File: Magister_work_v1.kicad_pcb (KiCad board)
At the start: 2 copper layers, 17 parts, among them J1 Conn_01x04_Pin, J2 Conn_01x03_Pin, J3 Conn_01x03_Pin, J4 Conn_01x03_Pin, J5 Conn_01x03_Pin, J6 Conn_01x04_Pin, U1 LM66100DCK, U2 XC6206P332MR

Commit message: feat: firs complete version schemattic
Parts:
- added C10: 10u, Capacitor_SMD:C_0805_2012Metric, F.Cu at (218.2, 74.2)
- added C11: 1u, Capacitor_SMD:C_0805_2012Metric, F.Cu at (218.2, 77.2)
- added C12: 15p, Capacitor_SMD:C_0805_2012Metric_Pad1.18x1.45mm_HandSolder, F.Cu at (212.0, 85.7)
- added C13: 15p, Capacitor_SMD:C_0805_2012Metric_Pad1.18x1.45mm_HandSolder, F.Cu at (212.0, 88.7)
- added C14: 10u, Capacitor_SMD:C_0805_2012Metric_Pad1.18x1.45mm_HandSolder, F.Cu at (212.0, 91.7)
- added C15: 1u, Capacitor_SMD:C_0805_2012Metric_Pad1.18x1.45mm_HandSolder, F.Cu at (212.0, 94.7)
- added C16: 1u, Capacitor_SMD:C_0805_2012Metric_Pad1.18x1.45mm_HandSolder, F.Cu at (212.0, 97.7)
- added C17: 1u, Capacitor_SMD:C_0805_2012Metric_Pad1.18x1.45mm_HandSolder, F.Cu at (212.0, 100.7)
- added C18: 0.1u, Capacitor_SMD:C_0805_2012Metric_Pad1.18x1.45mm_HandSolder, F.Cu at (212.0, 103.7)
- added C19: 2.2u, Capacitor_SMD:C_0805_2012Metric_Pad1.18x1.45mm_HandSolder, F.Cu at (212.0, 106.7)
- added C20: 0.1u, Capacitor_SMD:C_0805_2012Metric_Pad1.18x1.45mm_HandSolder, F.Cu at (174.4, 55.0)
- added C21: 0.1u, Capacitor_SMD:C_0805_2012Metric_Pad1.18x1.45mm_HandSolder, F.Cu at (174.4, 58.0)
- added C22: 22n, Capacitor_SMD:C_0805_2012Metric_Pad1.18x1.45mm_HandSolder, F.Cu at (174.4, 61.0)
- added C23: 0.1u, Capacitor_SMD:C_0805_2012Metric_Pad1.18x1.45mm_HandSolder, F.Cu at (174.4, 64.0)
- added C24: 0.1u, Capacitor_SMD:C_0805_2012Metric_Pad1.18x1.45mm_HandSolder, F.Cu at (174.4, 67.0)
- added C25: 0.1u, Capacitor_SMD:C_0805_2012Metric_Pad1.18x1.45mm_HandSolder, F.Cu at (174.4, 70.1)
- added C26: 0.1u, Capacitor_SMD:C_0805_2012Metric_Pad1.18x1.45mm_HandSolder, F.Cu at (174.4, 73.1)
- added C27: 0.1u, Capacitor_SMD:C_0805_2012Metric_Pad1.18x1.45mm_HandSolder, F.Cu at (174.4, 76.1)
- added C28: 0.1u, Capacitor_SMD:C_0805_2012Metric_Pad1.18x1.45mm_HandSolder, F.Cu at (174.4, 79.1)
- added C29: 0.1u, Capacitor_SMD:C_0805_2012Metric_Pad1.18x1.45mm_HandSolder, F.Cu at (222.9, 74.0)
- added C30: 0.1u, Capacitor_SMD:C_0805_2012Metric_Pad1.18x1.45mm_HandSolder, F.Cu at (222.9, 77.0)
- added C7: 10u, Capacitor_SMD:C_0805_2012Metric, F.Cu at (218.2, 65.2)
- added C8: 1u, Capacitor_SMD:C_0805_2012Metric, F.Cu at (218.2, 68.2)
- added C9: 10u, Capacitor_SMD:C_0805_2012Metric, F.Cu at (218.2, 71.2)
- added D2: SMBJ5.0CA, Diode_SMD:D_SMB_Handsoldering, F.Cu at (195.4, 80.8)
- added D3: SMBJ5.0CA, Diode_SMD:D_SMB_Handsoldering, F.Cu at (195.4, 86.3)
- added D4: BAT54C, Package_TO_SOT_SMD:SOT-23_Handsoldering, F.Cu at (212.8, 56.0)
- added DA1: K7803-500R3, Package_SIP:SIP3_11.6x8.5mm, F.Cu at (220.1, 60.8)
- added DD2: MPU-6050, Sensor_Motion:InvenSense_QFN-24_4x4mm_P0.5mm, F.Cu at (166.8, 94.0)
- added DD3: BMP280, Package_LGA:Bosch_LGA-8_2x2.5mm_P0.65mm_ClockwisePinNumbering, F.Cu at (202.9, 86.4)
- added J10: Conn_01x02_Pin, Connector_Hirose:Hirose_DF13-02P-1.25DSA_1x02_P1.25mm_Vertical, F.Cu at (227.7, 66.9)
- added J6: Conn_01x04_Pin, Connector_PinSocket_2.54mm:PinSocket_1x04_P2.54mm_Vertical, F.Cu at (216.7, 86.4)
- added J7: Conn_01x04_Pin, Connector_PinHeader_2.54mm:PinHeader_1x04_P2.54mm_Horizontal, F.Cu at (179.1, 74.8)
- added J8: Conn_01x06_Pin, Connector_Hirose:Hirose_DF13-06P-1.25DSA_1x06_P1.25mm_Vertical, F.Cu at (192.6, 75.8)
- added J9: Conn_01x02_Pin, Connector_Hirose:Hirose_DF13-02P-1.25DSA_1x02_P1.25mm_Vertical, F.Cu at (203.8, 75.8)
- added R1: 10k, Resistor_SMD:R_0805_2012Metric_Pad1.20x1.40mm_HandSolder, F.Cu at (221.3, 85.6)
- added R10: 1k, Resistor_SMD:R_0805_2012Metric_Pad1.20x1.40mm_HandSolder, F.Cu at (222.8, 68.1)
- added R11: 10k, Resistor_SMD:R_0805_2012Metric_Pad1.20x1.40mm_HandSolder, F.Cu at (222.8, 71.0)
- added R2: 10k, Resistor_SMD:R_0805_2012Metric_Pad1.20x1.40mm_HandSolder, F.Cu at (221.3, 88.6)
- added R3: 10k, Resistor_SMD:R_0805_2012Metric_Pad1.20x1.40mm_HandSolder, F.Cu at (221.3, 91.5)
- added R4: 3.3k, Resistor_SMD:R_0805_2012Metric_Pad1.20x1.40mm_HandSolder, F.Cu at (198.7, 55.0)
- added R5: 3.3k, Resistor_SMD:R_0805_2012Metric_Pad1.20x1.40mm_HandSolder, F.Cu at (198.7, 57.9)
- added R6: 3.3k, Resistor_SMD:R_0805_2012Metric_Pad1.20x1.40mm_HandSolder, F.Cu at (198.7, 60.9)
- added R7: 3.3k, Resistor_SMD:R_0805_2012Metric_Pad1.20x1.40mm_HandSolder, F.Cu at (198.7, 63.8)
- added R8: 3.3k, Resistor_SMD:R_0805_2012Metric_Pad1.20x1.40mm_HandSolder, F.Cu at (198.7, 66.8)
- added R9: 3k, Resistor_SMD:R_0805_2012Metric_Pad1.20x1.40mm_HandSolder, F.Cu at (222.8, 65.1)
- added U3: Ai-Thinker-Ra-01, RF_Module:Ai-Thinker-Ra-01-LoRa, F.Cu at (186.6, 63.0)
- added U4: MCP6001-OT, Package_TO_SOT_SMD:SOT-23-5, F.Cu at (239.9, 64.0)
- added VD1: GSOT03C-E3-08, Package_TO_SOT_SMD:SOT-23_Handsoldering, F.Cu at (204.3, 56.0)
- added VD2: GSOT03C-E3-08, Package_TO_SOT_SMD:SOT-23_Handsoldering, F.Cu at (204.3, 60.8)
- added VD3: GSOT03C-E3-08, Package_TO_SOT_SMD:SOT-23_Handsoldering, F.Cu at (204.3, 65.5)
- added VD4: GSOT03C-E3-08, Package_TO_SOT_SMD:SOT-23_Handsoldering, F.Cu at (212.8, 60.8)
- added VD5: GSOT03C-E3-08, Package_TO_SOT_SMD:SOT-23_Handsoldering, F.Cu at (212.8, 65.5)
- added VD6: GSOT03C-E3-08, Package_TO_SOT_SMD:SOT-23_Handsoldering, F.Cu at (212.8, 70.3)
- added VD7: GSOT03C-E3-08, Package_TO_SOT_SMD:SOT-23_Handsoldering, F.Cu at (212.8, 75.1)
- added VD8: GSOT03C-E3-08, Package_TO_SOT_SMD:SOT-23_Handsoldering, F.Cu at (212.8, 79.9)
- added Y1: X322525MQB4SI, Oscillator:Oscillator_SMD_Abracon_ASE-4Pin_3.2x2.5mm, F.Cu at (217.0, 98.6)
- C1: footprint Capacitor_SMD:C_0805_2012Metric -> Capacitor_SMD:C_0805_2012Metric_Pad1.18x1.45mm_HandSolder
- D1: footprint Diode_SMD:D_SMB -> Diode_SMD:D_SMB_Handsoldering
- F1: footprint Fuse:Fuse_1812_4532Metric -> Fuse:Fuse_1812_4532Metric_Pad1.30x3.40mm_HandSolder
- moved U1 103.5 mm to (145.8, 73.7)
- moved DD1 44.7 mm to (222.0, 125.5)
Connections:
- DD1 pad 1: unconnected-(DD1-VBAT-Pad1) -> +3V3D
- DD1 pad 12: unconnected-(DD1-VSSA-Pad12) -> GND
- DD1 pad 13: unconnected-(DD1-VREF+-Pad13) -> +3V3A
- DD1 pad 18: unconnected-(DD1-VSS-Pad18) -> GND
- DD1 pad 19: unconnected-(DD1-VDD-Pad19) -> +3V3D
- DD1 pad 28: unconnected-(DD1-PB2-Pad28) -> Net-(DD1-PB2)
- DD1 pad 30: unconnected-(DD1-VCAP1-Pad30) -> Net-(DD1-VCAP1)
- DD1 pad 31: unconnected-(DD1-VSS-Pad31) -> GND
- DD1 pad 32: unconnected-(DD1-VDD-Pad32) -> +3V3D
- DD1 pad 46: unconnected-(DD1-PA13-Pad46) -> Net-(DD1-PA13)
- DD1 pad 47: unconnected-(DD1-VSS-Pad47) -> GND
- DD1 pad 48: unconnected-(DD1-VDD-Pad48) -> +3V3D
- DD1 pad 49: unconnected-(DD1-PA14-Pad49) -> Net-(DD1-PA14)
- DD1 pad 5: unconnected-(DD1-PH0-Pad5) -> Net-(DD1-PH0)
- DD1 pad 6: unconnected-(DD1-PH1-Pad6) -> Net-(DD1-PH1)
- DD1 pad 60: unconnected-(DD1-BOOT0-Pad60) -> Net-(DD1-BOOT0)
- DD1 pad 63: unconnected-(DD1-VSS-Pad63) -> GND
- DD1 pad 64: unconnected-(DD1-VDD-Pad64) -> +3V3D
- DD1 pad 7: unconnected-(DD1-NRST-Pad7) -> Net-(DD1-NRST)

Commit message: feat: added all connection for MCU
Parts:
- removed the J6 at (199.7, 117.9)
- added D5: BAT54C, Package_TO_SOT_SMD:SOT-23_Handsoldering, F.Cu at (236.7, 111.0)
- added VD9: GSOT03C-E3-08, Package_TO_SOT_SMD:SOT-23_Handsoldering, F.Cu at (236.7, 115.8)
- U4: footprint Package_TO_SOT_SMD:SOT-23-5 -> Package_TO_SOT_SMD:SOT-23-5_HandSoldering
- moved J1 58.4 mm to (253.5, 120.9)
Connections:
- DD1 pad 14: unconnected-(DD1-PA0-Pad14) -> PWM1
- DD1 pad 15: unconnected-(DD1-PA1-Pad15) -> PWM2
- DD1 pad 16: unconnected-(DD1-PA2-Pad16) -> PWM3
- DD1 pad 17: unconnected-(DD1-PA3-Pad17) -> PWM4
- DD1 pad 21: unconnected-(DD1-PA5-Pad21) -> SCK_BMP280
- DD1 pad 22: unconnected-(DD1-PA6-Pad22) -> SDO_BMP280
- DD1 pad 23: unconnected-(DD1-PA7-Pad23) -> SDI_BMP280
- DD1 pad 24: unconnected-(DD1-PC4-Pad24) -> CSB_BMP280
- DD1 pad 26: unconnected-(DD1-PB0-Pad26) -> BAT_CTRL
- DD1 pad 29: unconnected-(DD1-PB10-Pad29) -> BN_880_SCL
- DD1 pad 33: unconnected-(DD1-PB12-Pad33) -> Reset_LoRa
- DD1 pad 34: unconnected-(DD1-PB13-Pad34) -> SCK_LoRa
- DD1 pad 35: unconnected-(DD1-PB14-Pad35) -> MISO_LoRa
- DD1 pad 36: unconnected-(DD1-PB15-Pad36) -> MOSI_LoRa
- DD1 pad 37: unconnected-(DD1-PC6-Pad37) -> SS_LoRa
- DD1 pad 38: unconnected-(DD1-PC7-Pad38) -> DIO0_LoRa
- DD1 pad 39: unconnected-(DD1-PC8-Pad39) -> DIO1_LoRa
- DD1 pad 40: unconnected-(DD1-PC9-Pad40) -> DIO2_LoRa
- DD1 pad 42: unconnected-(DD1-PA9-Pad42) -> BN_880_RX
- DD1 pad 43: unconnected-(DD1-PA10-Pad43) -> BN_880_TX
- DD1 pad 44: unconnected-(DD1-PA11-Pad44) -> TX_debug
- DD1 pad 45: unconnected-(DD1-PA12-Pad45) -> RX_debug
- DD1 pad 52: unconnected-(DD1-PC11-Pad52) -> HC_trigger
- DD1 pad 53: unconnected-(DD1-PC12-Pad53) -> HC_echo
- DD1 pad 55: unconnected-(DD1-PB3-Pad55) -> BN_880_SDA
- DD1 pad 57: unconnected-(DD1-PB5-Pad57) -> INT_MPU6050
- DD1 pad 58: unconnected-(DD1-PB6-Pad58) -> SCL_MPU6050
- DD1 pad 59: unconnected-(DD1-PB7-Pad59) -> SDA_MPU6050
- J1 pad 1: +5V -> Net-(J1-Pin_1)
- J1 pad 3: unconnected-(J1-Pin_3-Pad3) -> TX_debug
- J1 pad 4: unconnected-(J1-Pin_4-Pad4) -> RX_debug
- U3 pad 4: SS_LoRa -> Reset_LoRa
- U3 pad 5: MOSI_LoRa -> DIO0_LoRa
- U3 pad 6: MISO_LoRa -> DIO1_LoRa
- U3 pad 7: SCK_LoRa -> DIO2_LoRa

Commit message: feat: complete schematic, and start PCB
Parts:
- removed C26: 0.1u, Capacitor_SMD:C_0805_2012Metric_Pad1.18x1.45mm_HandSolder
- removed D1, D2, D3: SMBJ5.0CA, Diode_SMD:D_SMB_Handsoldering
- added C31: 0.1u, Capacitor_SMD:C_0805_2012Metric_Pad1.18x1.45mm_HandSolder, F.Cu at (153.9, 115.2)
- added C32: 0.1u, Capacitor_SMD:C_0805_2012Metric_Pad1.18x1.45mm_HandSolder, F.Cu at (153.9, 118.2)
- added D6: SMBJ5.0CA, Diode_SMD:D_SMB_Handsoldering, F.Cu at (94.0, 33.5)
- added D7: SMBJ5.0CA, Diode_SMD:D_SMB_Handsoldering, F.Cu at (46.5, 118.0)
- added D8: SMBJ5.0CA, Diode_SMD:D_SMB_Handsoldering, F.Cu at (39.0, 101.0)
- added D9: BAT54C, Package_TO_SOT_SMD:SOT-23_Handsoldering, F.Cu at (155.7, 105.5)
- added L1: BLM21PG121SN1D, Inductor_SMD:L_0805_2012Metric_Pad1.05x1.20mm_HandSolder, F.Cu at (160.8, 112.3)
- added L2: BLM21PG121SN1D, Inductor_SMD:L_0805_2012Metric_Pad1.05x1.20mm_HandSolder, F.Cu at (153.9, 112.3)
- C10, C11, C2, C3, C4, C5, C6, C7, C8, C9: footprint Capacitor_SMD:C_0805_2012Metric -> Capacitor_SMD:C_0805_2012Metric_Pad1.18x1.45mm_HandSolder
- C16, C17: value 1u -> 0.1u
- U2: footprint Package_TO_SOT_SMD:SOT-23-3 -> Package_TO_SOT_SMD:SOT-23_Handsoldering
- moved J1 224.5 mm to (32.0, 84.3), turned to 180 degrees
- moved U2 211.4 mm to (41.0, 31.5)
- moved J10 195.7 mm to (32.0, 69.5), turned to 90 degrees
- moved U4 194.7 mm to (45.1, 65.5), turned to 180 degrees
- moved C6 180.8 mm to (34.0, 32.0), turned to 90 degrees
- moved J9 172.6 mm to (32.0, 91.8), turned to 90 degrees
- moved DA1 170.4 mm to (52.2, 31.5), turned to -90 degrees
- moved C5 168.3 mm to (46.5, 32.0), turned to -90 degrees
- moved J8 163.1 mm to (32.0, 104.1), turned to 90 degrees
- moved DD1 159.6 mm to (67.0, 87.5)
- moved C7 158.0 mm to (63.5, 33.5), turned to 90 degrees
- moved DD3 157.1 mm to (50.0, 50.2)
- moved C8 155.2 mm to (67.0, 33.5), turned to 90 degrees
- moved F1 150.0 mm to (100.5, 30.5)
- moved J7 146.0 mm to (40.0, 119.1), turned to 180 degrees
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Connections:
- C1 pad 1: Net-(D1-A2) -> Net-(D6-A2)
- C17 pad 1: +3V3D -> +3V3_MCU
- C2 pad 1: Net-(D1-A2) -> Net-(D6-A2)
- C3 pad 1: Net-(D1-A2) -> Net-(D6-A2)
- DD1 pad 1: +3V3D -> +3V3_MCU
- DD1 pad 19: +3V3D -> +3V3_MCU
- DD1 pad 32: +3V3D -> +3V3_MCU
- DD1 pad 48: +3V3D -> +3V3_MCU
- DD1 pad 64: +3V3D -> +3V3_MCU
- F1 pad 1: (no net) -> +5V_1
- F1 pad 2: (no net) -> Net-(D6-A2)
- J6 pad 1: +3V3D -> Net-(J6-Pin_1)
- J6 pad 2: GND -> Net-(DD1-PA13)
- J6 pad 3: Net-(DD1-PA13) -> Net-(DD1-PA14)
- J6 pad 4: Net-(DD1-PA14) -> GND
- U1 pad 1: Net-(D1-A2) -> Net-(D6-A2)
- U3 pad 3: +3V3D -> Net-(U3-VDD)
- VD9 pad 1: TX_debug -> RX_debug
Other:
- board outline added: 100 x 100 mm

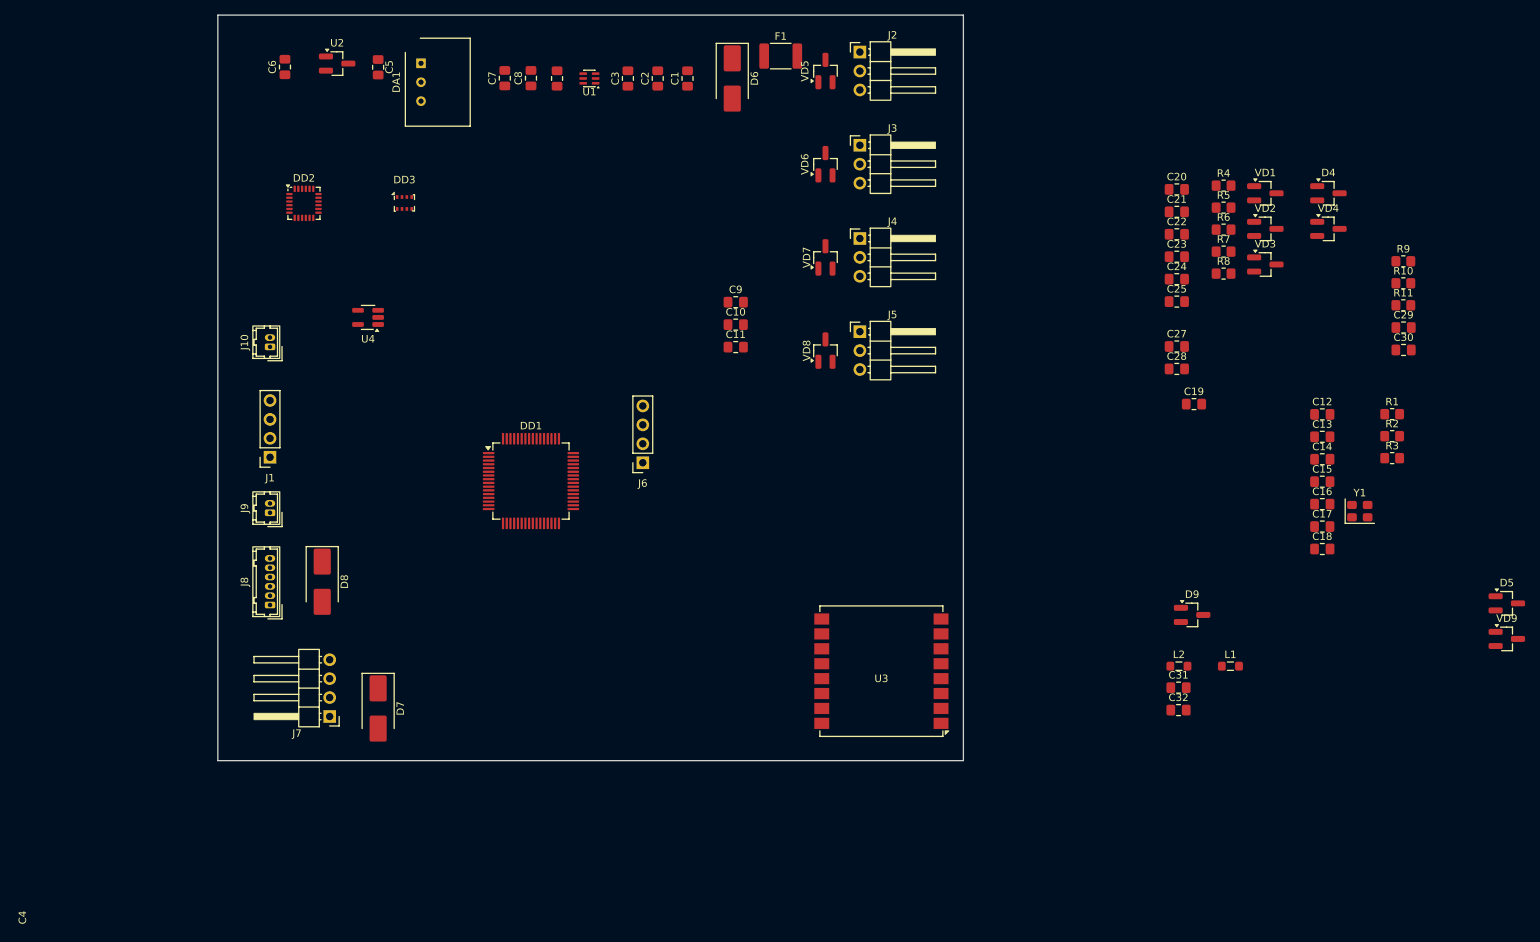
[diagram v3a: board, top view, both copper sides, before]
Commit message: feat: first version pf PCB without data and power line
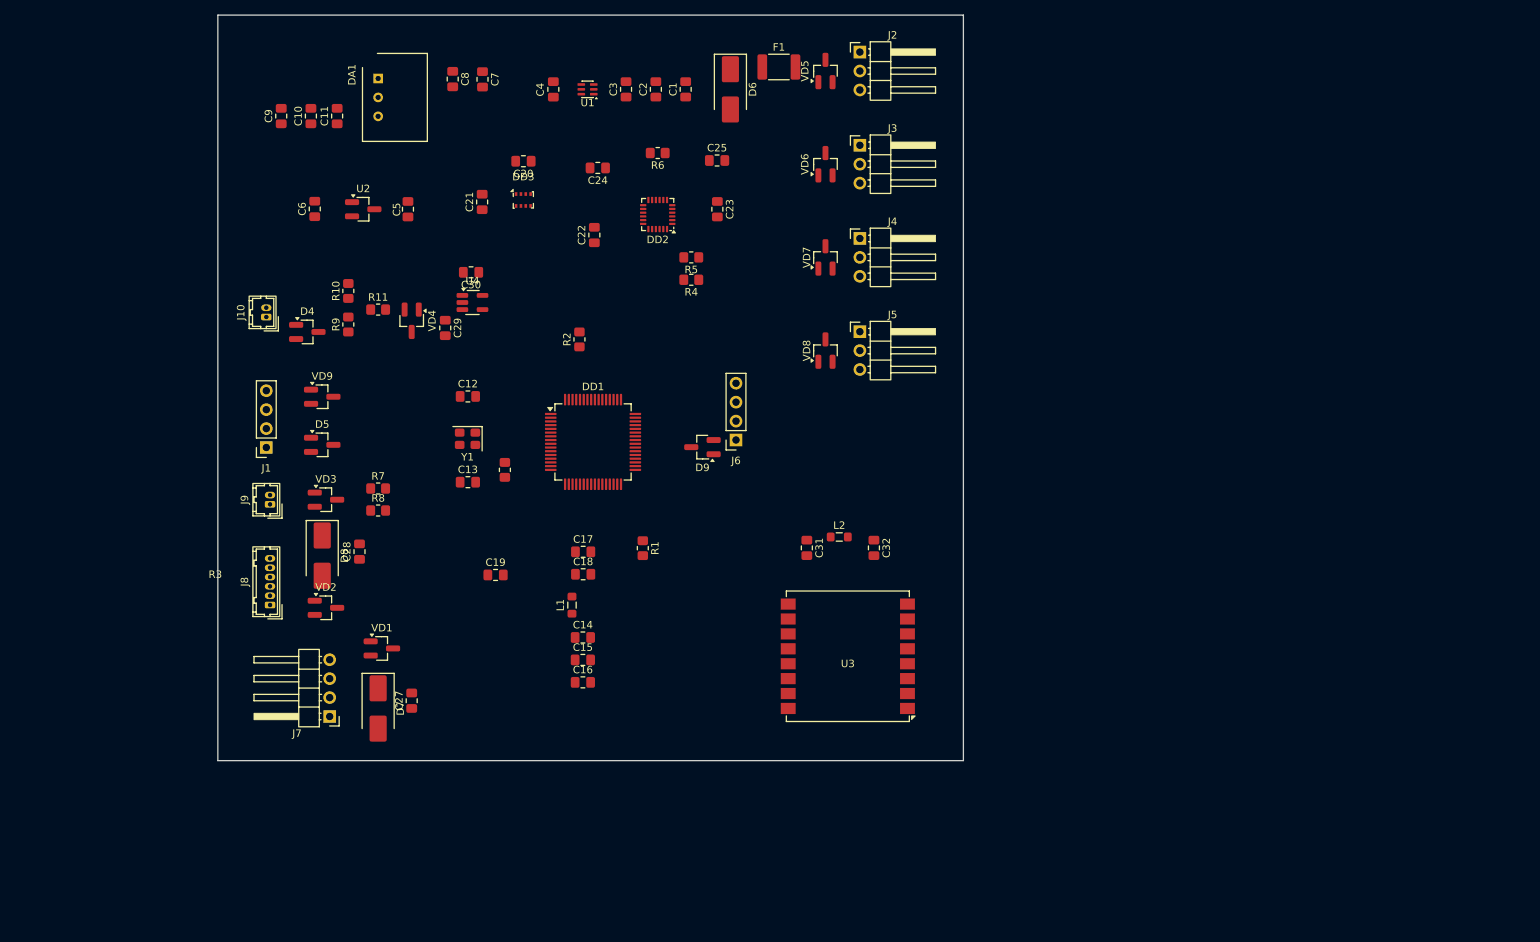
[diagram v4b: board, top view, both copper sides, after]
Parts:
- moved VD9 162.2 mm to (39.0, 76.2)
- moved D5 160.3 mm to (39.0, 82.6)
- moved R9 141.8 mm to (42.5, 66.5), turned to 90 degrees
- moved R10 141.5 mm to (42.5, 62.0), turned to 90 degrees
- moved D4 138.2 mm to (37.0, 67.5)
- moved R11 137.5 mm to (46.5, 64.5)
- moved VD2 135.9 mm to (39.5, 104.5)
- moved VD1 133.3 mm to (47.0, 110.0)
- moved VD3 129.9 mm to (39.5, 90.0)
- moved C29 128.5 mm to (55.5, 67.0), turned to -90 degrees
- moved C30 125.5 mm to (59.0, 59.5), turned to 180 degrees
- moved VD4 123.6 mm to (51.0, 66.0), turned to -90 degrees
- moved Y1 120.1 mm to (58.5, 81.8), turned to 180 degrees
- moved R3 119.0 mm to (63.5, 86.0), turned to 90 degrees
- moved R7 117.8 mm to (46.5, 88.5)
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
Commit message: feat: start PCB trace
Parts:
- moved L2 16.6 mm to (119.5, 107.3), turned to -90 degrees
- moved C32 16.3 mm to (118.0, 112.0), turned to 180 degrees
- moved C31 15.5 mm to (118.0, 103.0), turned to 180 degrees
- moved D9 13.7 mm to (103.5, 85.5), turned to 0 degrees
- moved C18 13.2 mm to (65.5, 90.0), turned to 90 degrees
- moved C6 13.0 mm to (51.0, 50.1), turned to -90 degrees
- moved R3 8.66 mm to (65.5, 94.4)
- moved C5 8.56 mm to (42.0, 50.0), turned to -90 degrees
- moved L1 6.77 mm to (78.5, 101.0), turned to 0 degrees
- moved DD1 6.72 mm to (82.0, 83.0)
- moved C14 5.43 mm to (78.5, 105.5)
- moved VD5 5.02 mm to (107.0, 37.5), turned to -90 degrees
- moved C15 4.92 mm to (78.5, 109.5)
- moved C16 4.92 mm to (78.5, 112.5)
- moved J6 4.72 mm to (98.5, 84.5)
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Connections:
- net Net-(D6-A2) renamed +5V_2
- R10 pad 1: Net-(VD4-K1) -> Net-(R10-Pad1)
- R11 pad 1: Net-(VD4-K1) -> Net-(R10-Pad1)
- R9 pad 2: Net-(VD4-K1) -> Net-(R10-Pad1)
- VD4 pad 1: Net-(VD4-K1) -> Net-(U4-+)
- VD4 pad 2: Net-(VD4-K1) -> Net-(U4-+)
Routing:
- net +5V: track 0.00 -> 65.2 mm
- net +5V_1: track 0.00 -> 56.9 mm
- net GND: track 0.00 -> 47.1 mm
- net +5V_2: track 0.00 -> 28.1 mm
- net +3V3D: track 0.00 -> 16.8 mm
- net Net-(U4-+): track 0.00 -> 14.6 mm
- net BAT_CTRL: track 0.00 -> 12.8 mm
- net Net-(U3-VDD): track 0.00 -> 11.7 mm
- net Net-(J1-Pin_1): track 0.00 -> 8.14 mm
- net BN_880_TX: track 0.00 -> 7.11 mm
- net HC_trigger: track 0.00 -> 6.84 mm
- net BN_880_RX: track 0.00 -> 6.80 mm
- net HC_echo: track 0.00 -> 6.52 mm
- net TX_debug: track 0.00 -> 6.32 mm
- net BN_880_SDA: track 0.00 -> 6.13 mm
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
